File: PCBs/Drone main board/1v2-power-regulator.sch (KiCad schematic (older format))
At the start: 9 parts, among them U501 AP63200WU-7

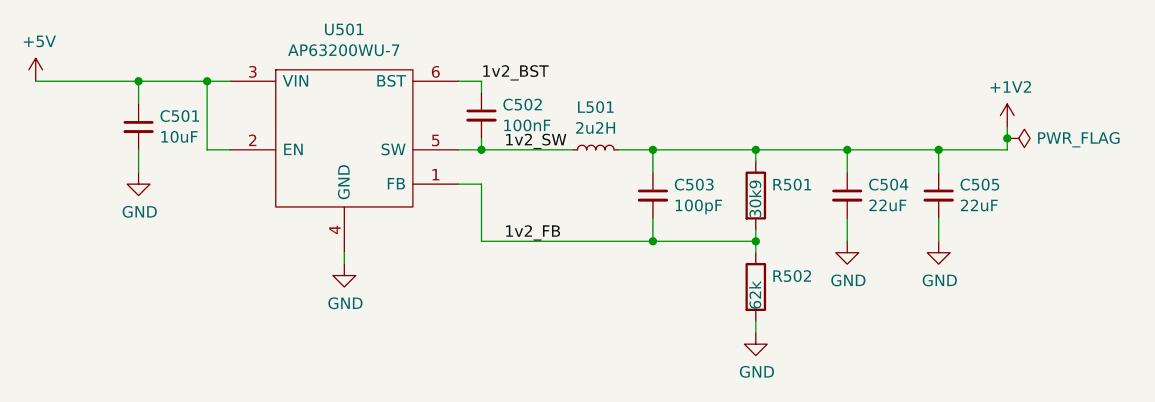
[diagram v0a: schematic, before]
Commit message: Added PDFs of schematics. Corrected a few value labels in drone schematic.
Signed-off-by: Eldalote.Electronics <Eldalote.Electronics@gmail.com>
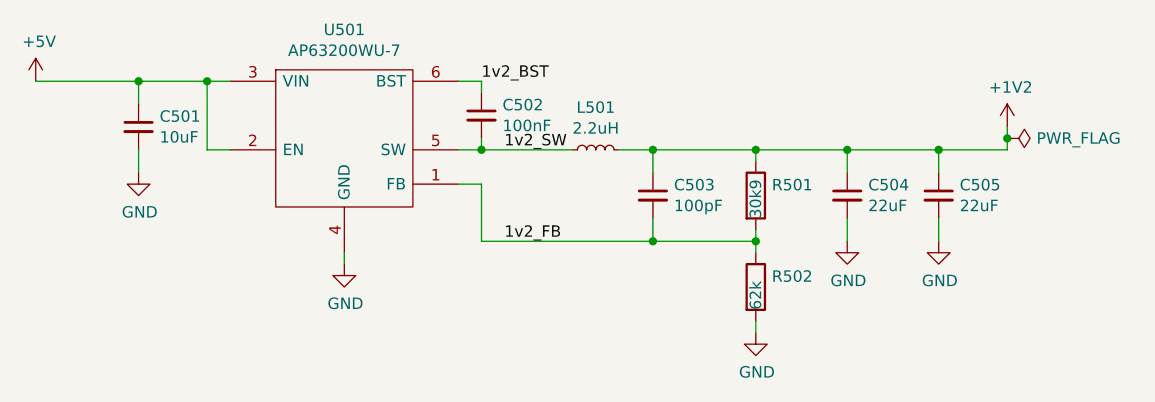
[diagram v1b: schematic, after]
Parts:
- L501: value 2u2H -> 2.2uH
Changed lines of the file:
@@
 P 5800 3350
 F 0 "L501" V 5985 3350 50  0000 C CNN
-F 1 "2u2H" V 5894 3350 50  0000 C CNN
+F 1 "2.2uH" V 5894 3350 50  0000 C CNN
 F 2 "Eldalote-footprints:L_4018_Bourns" H 5800 3350 50  0001 C CNN
 F 3 "~" H 5800 3350 50  0001 C CNN

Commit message: Lots of work to check every component, add Manufacturers number (instead of LCSC or digikey and mouser numbers)
Changed to USB-C connector, almost done with that sheet. Components checked, need to redo Sheet IO

Signed-off-by: Eldalote.Electronics <Eldalote.Electronics@gmail.com>
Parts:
- C501: LCSC C15850 -> (none); MfNr (none) -> CL21A106KAYNNNG
- C502: LCSC C1525 -> (none); MfNr (none) -> CL05B104KO5NNNC
- C503: LCSC C1546 -> (none); MfNr (none) -> CL05C101JB5NNN
- C504, C505: LCSC C45783 -> (none); MfNr (none) -> CL21A226MAQNNNE
- L501: DigiKey SRN4018-2R2MCT-ND -> (none); MfNr (none) -> SRN4018-2R2M; Mouser 652-SRN4018-2R2M -> (none)
- R501: footprint Resistor_SMD:R_0805_2012Metric_Pad1.15x1.40mm_HandSolder -> Resistor_SMD:R_0402_1005Metric; DigiKey P30.9KCCT-ND -> (none); MfNr (none) -> RK73H1ETTP3092F; Mouser 667-ERJ-6ENF3092V -> (none)
- R502: footprint Resistor_SMD:R_0805_2012Metric -> Resistor_SMD:R_0402_1005Metric; LCSC C17783 -> (none); MfNr (none) -> ERJ-2RKF6202X
- U501: MfNr (none) -> AP63200WU-7
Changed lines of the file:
@@
 F 2 "SOT95P280X100-6N" H 5050 3650 50  0001 L CNN
 F 3 "https://www.diodes.com/assets/Datasheets/AP63200-AP63201-AP63203-AP63205.pdf" H 5050 3550 50  0001 L CNN
+F 4 "AP63200WU-7" H 4200 3100 50  0001 C CNN "MfNr"
 	1    4200 3100
 	1    0    0    -1
@@
 F 2 "Capacitor_SMD:C_0805_2012Metric" H 3800 3250 50  0001 C CNN
 F 3 "~" H 3800 3250 50  0001 C CNN
-F 4 "C15850" H 3800 3250 50  0001 C CNN "LCSC"
+F 4 "CL21A106KAYNNNG" H 3800 3250 50  0001 C CNN "MfNr"
 	1    3800 3250
 	1    0    0    -1
@@
 F 2 "Capacitor_SMD:C_0402_1005Metric" H 5300 3200 50  0001 C CNN
 F 3 "~" H 5300 3200 50  0001 C CNN
-F 4 "C1525" H 5300 3200 50  0001 C CNN "LCSC"
+F 4 "CL05B104KO5NNNC" H 5300 3200 50  0001 C CNN "MfNr"
 	1    5300 3200
 	1    0    0    -1
@@
 F 2 "Capacitor_SMD:C_0402_1005Metric" H 6050 3550 50  0001 C CNN
 F 3 "~" H 6050 3550 50  0001 C CNN
-F 4 "C1546" H 6050 3550 50  0001 C CNN "LCSC"
+F 4 "CL05C101JB5NNN" H 6050 3550 50  0001 C CNN "MfNr"
 	1    6050 3550
 	1    0    0    -1
@@
 F 2 "Capacitor_SMD:C_0805_2012Metric" H 6900 3550 50  0001 C CNN
 F 3 "~" H 6900 3550 50  0001 C CNN
-F 4 "C45783" H 6900 3550 50  0001 C CNN "LCSC"
+F 4 "CL21A226MAQNNNE" H 6900 3550 50  0001 C CNN "MfNr"
 	1    6900 3550
 	1    0    0    -1
@@
 F 2 "Eldalote-footprints:L_4018_Bourns" H 5800 3350 50  0001 C CNN
 F 3 "~" H 5800 3350 50  0001 C CNN
-F 4 "652-SRN4018-2R2M" V 5800 3350 50  0001 C CNN "Mouser"
-F 5 "SRN4018-2R2MCT-ND" V 5800 3350 50  0001 C CNN "DigiKey"
+F 4 "SRN4018-2R2M" V 5800 3350 50  0001 C CNN "MfNr"
 	1    5800 3350
 	0    -1   -1   0
@@
 F 0 "R501" H 6570 3596 50  0000 L CNN
 F 1 "30k9" V 6500 3450 50  0000 L CNN
-F 2 "Resistor_SMD:R_0805_2012Metric_Pad1.15x1.40mm_HandSolder" V 6430 3550 50  0001 C CNN
+F 2 "Resistor_SMD:R_0402_1005Metric" V 6430 3550 50  0001 C CNN
 F 3 "~" H 6500 3550 50  0001 C CNN
-F 4 "667-ERJ-6ENF3092V " H 6500 3550 50  0001 C CNN "Mouser"
-F 5 "P30.9KCCT-ND " H 6500 3550 50  0001 C CNN "DigiKey"
+F 4 "RK73H1ETTP3092F" H 6500 3550 50  0001 C CNN "MfNr"
 	1    6500 3550
 	1    0    0    -1
@@
 F 0 "R502" H 6570 3996 50  0000 L CNN
 F 1 "62k" V 6500 3850 50  0000 L CNN
-F 2 "Resistor_SMD:R_0805_2012Metric" V 6430 3950 50  0001 C CNN
+F 2 "Resistor_SMD:R_0402_1005Metric" V 6430 3950 50  0001 C CNN
 F 3 "~" H 6500 3950 50  0001 C CNN
-F 4 "C17783" H 6500 3950 50  0001 C CNN "LCSC"
+F 4 "ERJ-2RKF6202X" H 6500 3950 50  0001 C CNN "MfNr"
 	1    6500 3950
 	1    0    0    -1
@@
 F 2 "Capacitor_SMD:C_0805_2012Metric" H 7300 3550 50  0001 C CNN
 F 3 "~" H 7300 3550 50  0001 C CNN
-F 4 "C45783" H 7300 3550 50  0001 C CNN "LCSC"
+F 4 "CL21A226MAQNNNE" H 7300 3550 50  0001 C CNN "MfNr"
 	1    7300 3550
 	1    0    0    -1
